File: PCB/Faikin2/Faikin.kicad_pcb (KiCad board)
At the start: 2 copper layers, 70 x 70 mm, 25 parts, among them J1 1x5, J2 Shelly, J3 USB-PROG, Q1 BSS138PS, U3 MD8942, U4 ESP32-S3-MINI-1

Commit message: Rework reg
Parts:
- moved R11 1.29 mm to (145.7, 71.0), turned to 180 degrees
- moved R10 1.29 mm to (142.1, 71.0), turned to 180 degrees
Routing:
- net DC: track 18.1 -> 19.0 mm
- net GND: vias 26 -> 28

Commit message: Added cap
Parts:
- added C1: 100nF, RevK:C_0402, F.Cu at (147.9, 58.2)

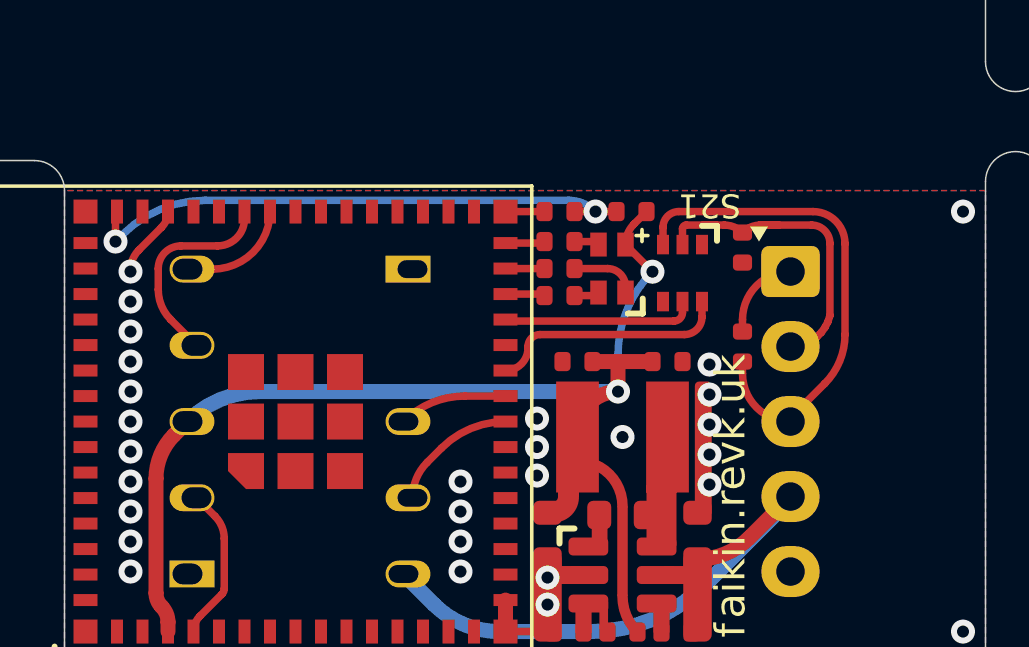
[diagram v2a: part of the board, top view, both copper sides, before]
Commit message: Removed cap, tests show it makes matters worse
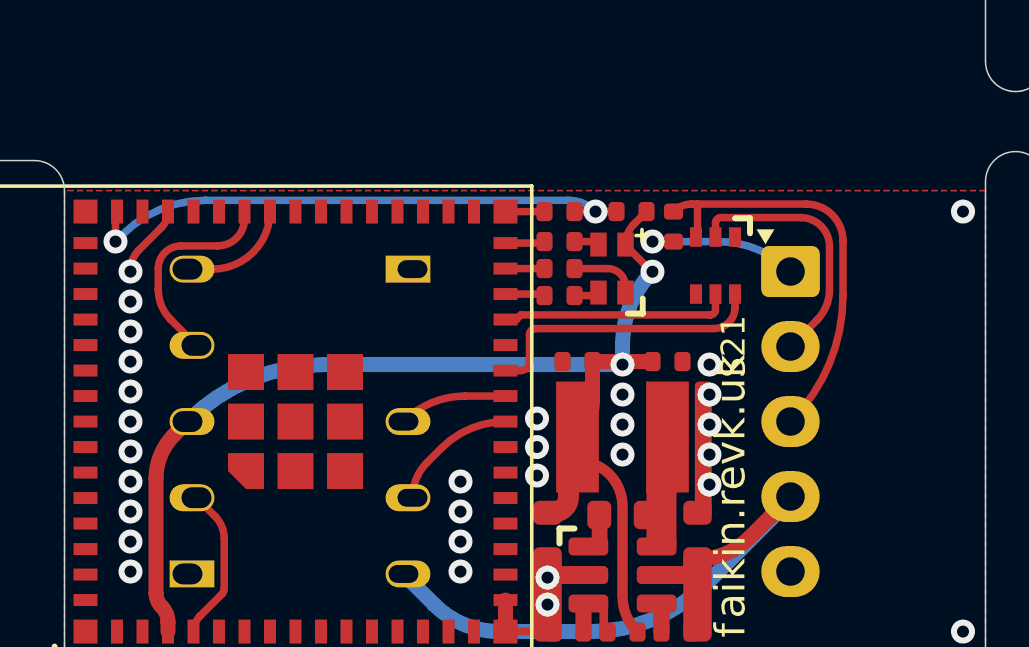
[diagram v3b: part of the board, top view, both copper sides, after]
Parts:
- removed C1: 100nF, RevK:C_0402
- moved R1 4.61 mm to (145.6, 57.5), turned to 90 degrees
- moved Q1 1.13 mm to (147.0, 58.8)
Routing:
- net Net-(J1-Pin_3): track 16.8 -> 13.9 mm
- net Net-(J1-Pin_1): track 2.85 -> 5.55 mm, vias 0 -> 1
- net Net-(J1-Pin_2): track 10.5 -> 8.79 mm
- net RX: track 8.03 -> 9.64 mm
- net TX: track 6.37 -> 7.68 mm
- net +3.3V: track 34.0 -> 33.0 mm
- net GND: vias 28 -> 30

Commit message: More tidy
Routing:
- net DC: track 18.9 -> 20.2 mm

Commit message: Cut out tidy
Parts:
- added Z1: Hidden, RevK:PCB-Join, F.Cu at (110.0, 71.8)
- added Z2: Hidden, RevK:PCB-Join, F.Cu at (110.0, 56.2)
- added Z3: Hidden, RevK:PCB-Join, F.Cu at (157.0, 54.0)
- added Z4: Hidden, RevK:PCB-Join, F.Cu at (157.0, 74.0)
- added Z5: Hidden, RevK:PCB-Join, F.Cu at (120.0, 83.0)
- added Z6: Hidden, RevK:PCB-Join, F.Cu at (147.0, 83.0)
- added Z7: Hidden, RevK:PCB-Join, F.Cu at (147.0, 45.0)
- added Z8: Hidden, RevK:PCB-Join, F.Cu at (120.0, 45.0)

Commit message: Snap out
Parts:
- Z1, Z2, Z3, Z4, Z5, Z6, Z7, Z8: footprint RevK:PCB-Join -> RevK:PCB-Join1
- turned Z3 to 180 degrees
- turned Z4 to 180 degrees
- turned Z7 to -90 degrees
- turned Z8 to -90 degrees
